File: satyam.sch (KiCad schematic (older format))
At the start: 4 parts, among them J1 Conn_01x02, U1 supermcu1

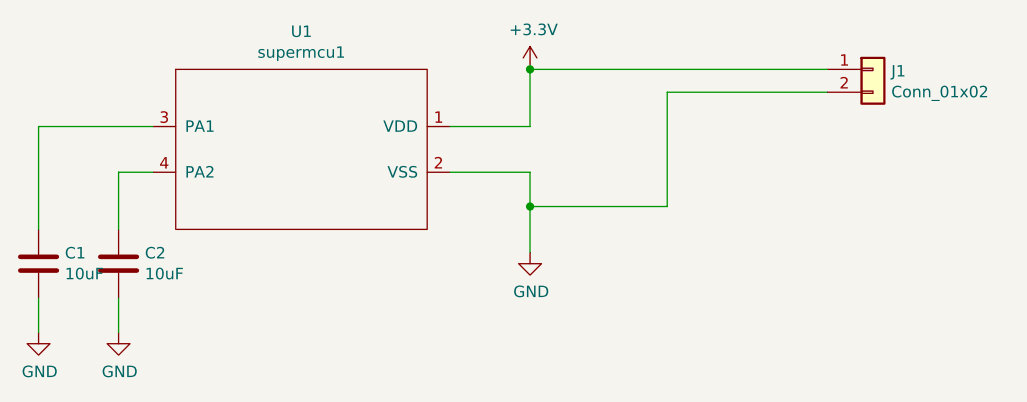
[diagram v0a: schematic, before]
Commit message: Change C1 to 30uF
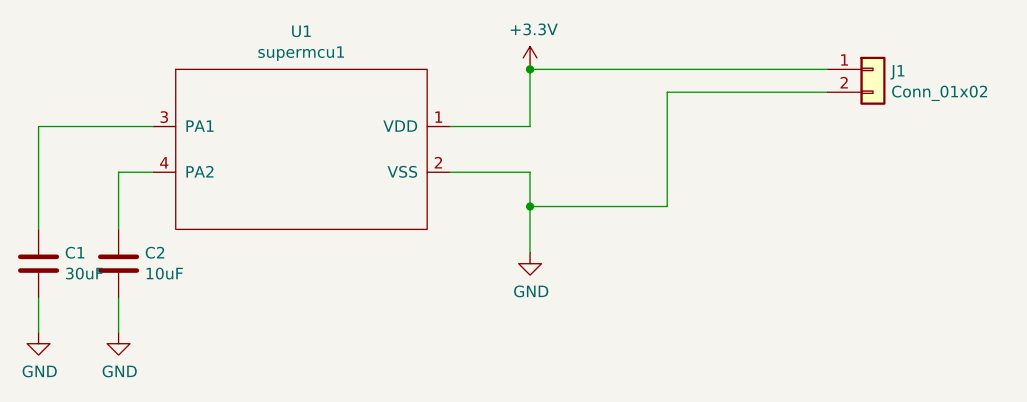
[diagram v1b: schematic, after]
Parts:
- C1: value 10uF -> 30uF
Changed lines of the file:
@@
 P 3900 3500
 F 0 "C1" H 4015 3546 50  0000 L CNN
-F 1 "10uF" H 4015 3455 50  0000 L CNN
+F 1 "30uF" H 4015 3455 50  0000 L CNN
 F 2 "Capacitor_SMD:C_0805_2012Metric" H 3938 3350 50  0001 C CNN
 F 3 "~" H 3900 3500 50  0001 C CNN
